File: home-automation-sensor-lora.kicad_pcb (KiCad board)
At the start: 4 copper layers, 96.5 x 96.5 mm, 126 parts, among them J1 Thermistor, J2 Conn_01x08, J3 Stemma-QT-Connector, J4 USB4105-GF-A_Lizard, J5 3V3-16V, J6 Conn_01x04, Q1 DMN2046U-7, Q2 DMN2046U-7, Q3 DMG3415U-7, U1 LD2985BM33R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

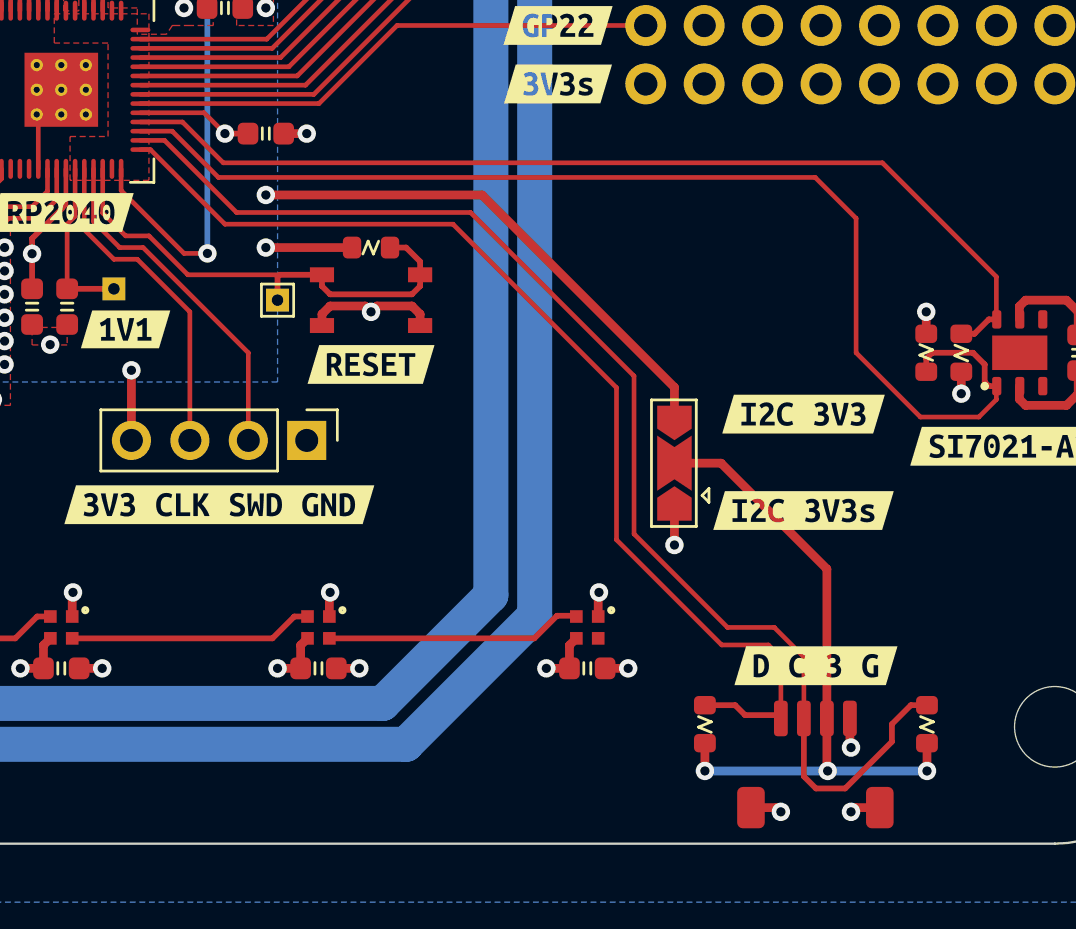
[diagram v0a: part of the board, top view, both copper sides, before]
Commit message: corrected mirrored stemma qt connector pinout
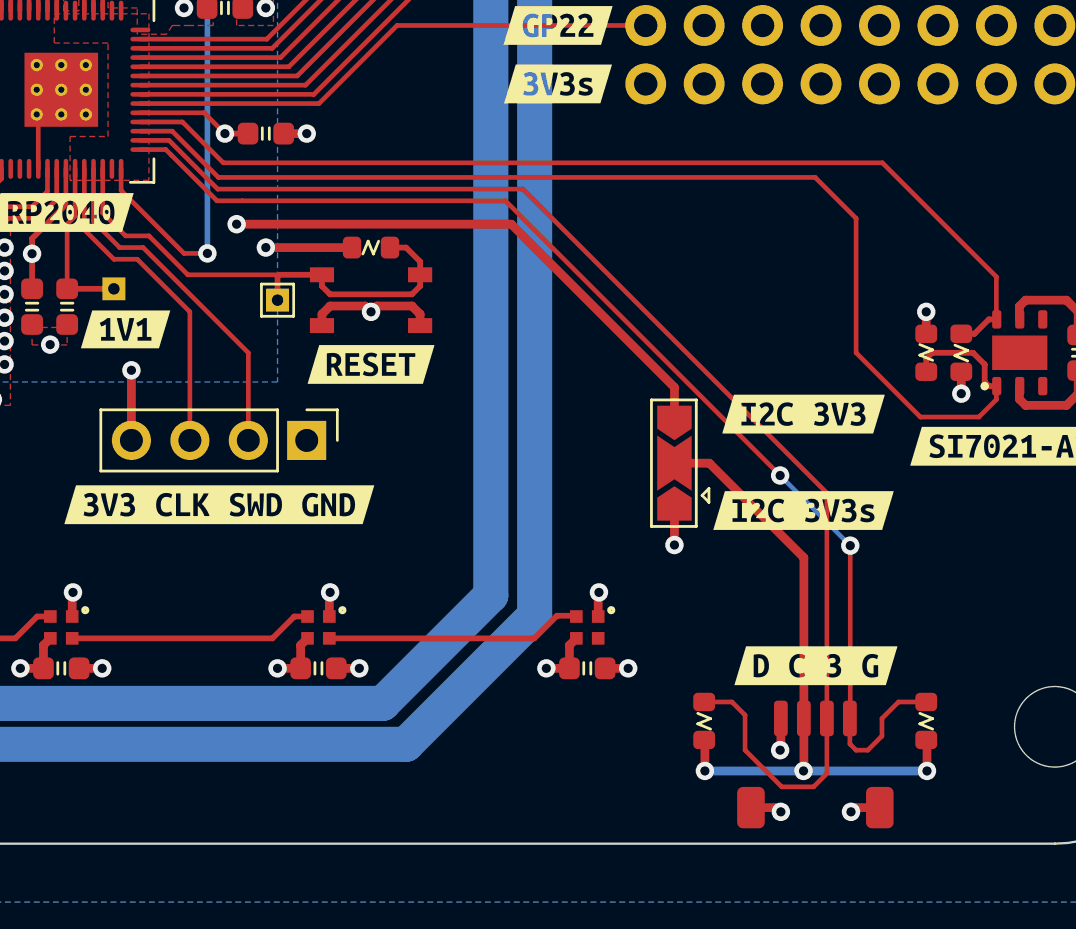
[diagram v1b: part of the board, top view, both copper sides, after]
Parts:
- moved R14 9.69 mm to (198.7, 122.5)
- moved R15 9.62 mm to (208.3, 122.5)
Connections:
- J3 pad 1: SDA1 -> GND
- J3 pad 2: SCL1 -> /QT Power
- J3 pad 3: /QT Power -> SCL1
- J3 pad 4: GND -> SDA1
- U5 pad 11: LORA_MISO -> unconnected-(U5-GPIO8-Pad11)
- U5 pad 4: unconnected-(U5-GPIO2-Pad4) -> LORA_RESET
- U5 pad 6: LORA_RESET -> LORA_MISO
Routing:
- net SDA1: track 46.8 -> 51.3 mm, vias 0 -> 2
- net SCL1: track 54.9 -> 56.4 mm
- net +3V3: track 53.3 -> 54.1 mm
- net /QT Power: track 29.4 -> 28.7 mm

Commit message: updated resistor values
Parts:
- R1, R10: value 1k -> 2k7
- R12: value 2.7k -> 2k7
- R14, R15: value 10k -> 2k7
- R5, R6, R7: value 5.1k -> 5k1
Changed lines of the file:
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@@
         (effects (font (size 1 1) (thickness 0.15)))
     )
-    (fp_text value "2.7k" (at 0 1.43) (layer "F.Fab")
+    (fp_text value "2k7" (at 0 1.43) (layer "F.Fab")
         (effects (font (size 1 1) (thickness 0.15)))
     )
@@
         (effects (font (size 1 1) (thickness 0.15)))
     )
-    (fp_text value "10k" (at 0 1.43 90) (layer "F.Fab")
+    (fp_text value "2k7" (at 0 1.43 90) (layer "F.Fab")
         (effects (font (size 1 1) (thickness 0.15)))
     )
@@
         (effects (font (size 1 1) (thickness 0.15)))
     )
-    (fp_text value "5.1k" (at 0 1.43 90) (layer "F.Fab")
+    (fp_text value "5k1" (at 0 1.43 90) (layer "F.Fab")
         (effects (font (size 1 1) (thickness 0.15)))
     )
@@
         (effects (font (size 1 1) (thickness 0.15)))
     )
-    (fp_text value "10k" (at 0 1.43 90) (layer "F.Fab")
+    (fp_text value "2k7" (at 0 1.43 90) (layer "F.Fab")
         (effects (font (size 1 1) (thickness 0.15)))
     )
@@
         (effects (font (size 1 1) (thickness 0.15)))
     )
-    (fp_text value "5.1k" (at 0 1.43 90) (layer "F.Fab")
+    (fp_text value "5k1" (at 0 1.43 90) (layer "F.Fab")
         (effects (font (size 1 1) (thickness 0.15)))
     )
@@
         (effects (font (size 1 1) (thickness 0.15)))
     )
-    (fp_text value "1k" (at 0 1.43) (layer "F.Fab")
+    (fp_text value "2k7" (at 0 1.43) (layer "F.Fab")
         (effects (font (size 1 1) (thickness 0.15)))
     )
@@
         (effects (font (size 1 1) (thickness 0.15)))
     )
-    (fp_text value "1k" (at 0 1.43) (layer "F.Fab")
+    (fp_text value "2k7" (at 0 1.43) (layer "F.Fab")
         (effects (font (size 1 1) (thickness 0.15)))
     )
@@
         (effects (font (size 1 1) (thickness 0.15)))
     )
-    (fp_text value "5.1k" (at 0 1.43 90) (layer "F.Fab")
+    (fp_text value "5k1" (at 0 1.43 90) (layer "F.Fab")
         (effects (font (size 1 1) (thickness 0.15)))
     )

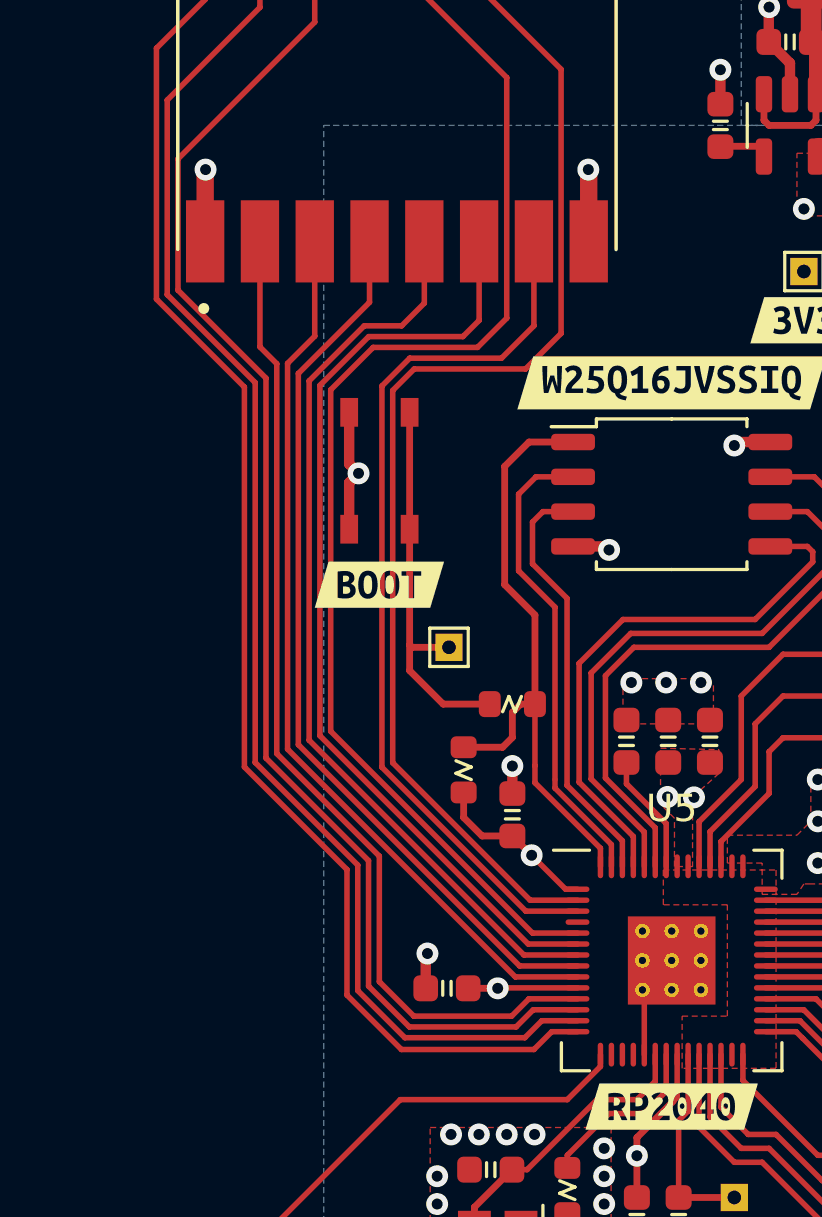
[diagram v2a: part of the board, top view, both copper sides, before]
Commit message: fixed routing to lora module
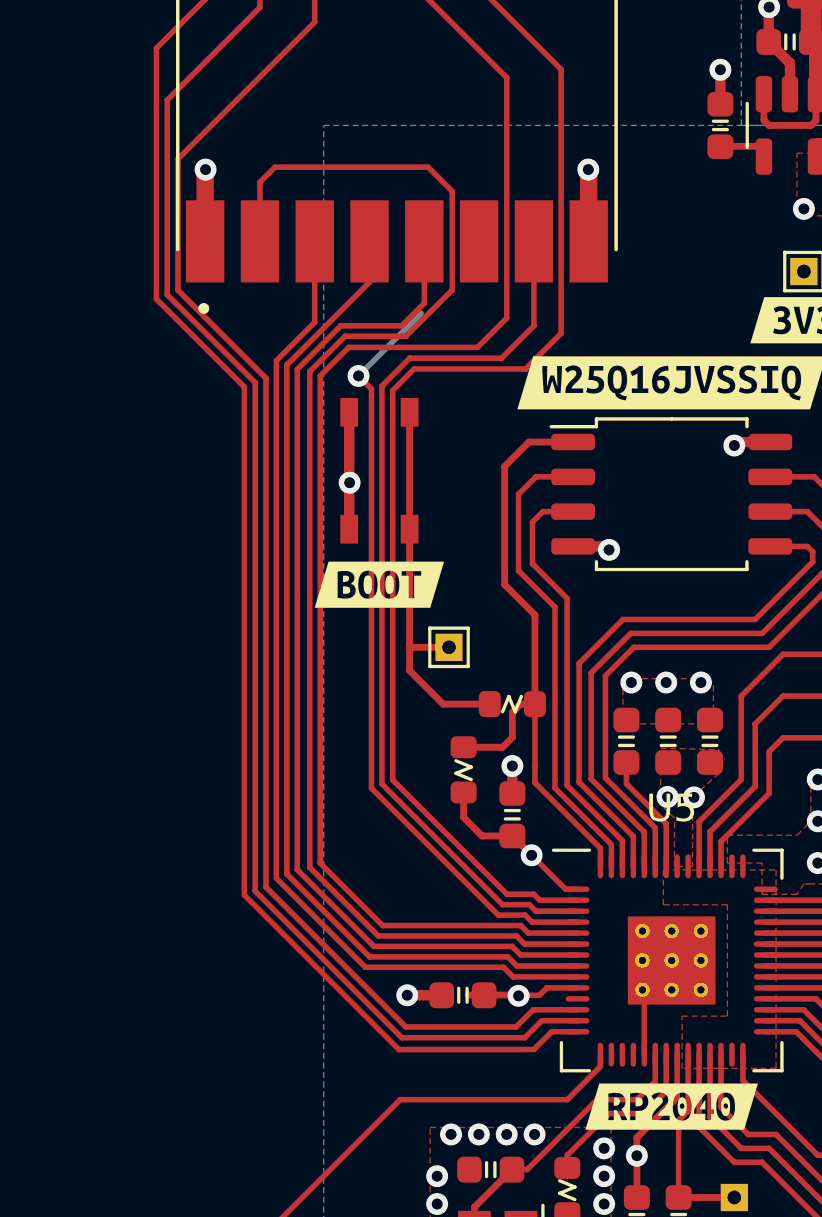
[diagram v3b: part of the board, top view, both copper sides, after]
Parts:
- moved C12 0.64 mm to (163.1, 96.3)
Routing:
- net LORA_MISO: track 36.8 -> 48.8 mm
- net LORA_RESET: track 35.0 -> 28.0 mm, vias 0 -> 1
- net LORA_NSS: track 33.8 -> 37.7 mm
- net LORA_DIO4: track 51.5 -> 55.4 mm
- net LORA_SCK: track 33.0 -> 36.3 mm
- net LORA_MOSI: track 33.0 -> 36.3 mm
- net GND: track 67.9 -> 67.4 mm

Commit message: updated BMS to auto-start version
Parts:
- U7: value AP9101CK6-ANTRG1 -> AP9101CAK6-ANTRG1
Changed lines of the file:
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@@
   (net 73 "unconnected-(U4-DNC-Pad4)")
   (net 74 "unconnected-(U4-PAD-Pad7)")
-  (net 75 "Net-(#FLG0103-pwr)")
+  (net 75 "Net-(U2-VIN)")
   (net 76 "unconnected-(U5-GPIO13-Pad16)")
   (net 77 "unconnected-(U5-GPIO14-Pad17)")
   (net 78 "unconnected-(U5-GPIO15-Pad18)")
   (net 79 "unconnected-(U5-GPIO16-Pad27)")
-  (net 80 "Net-(#FLG0101-pwr)")
+  (net 80 "Net-(U1-EN)")
   (net 81 "unconnected-(U5-GPIO8-Pad11)")
   (footprint "lizard_libs:R_0603_Lizard" (layer "F.Cu")
@@
       (stroke (width 0.1) (type solid)) (layer "F.Fab"))
     (pad "1" smd roundrect (at -1.1375 -0.95 270) (size 1.325 0.6) (layers "F.Cu" "F.Paste" "F.Mask") (roundrect_rratio 0.25)
-      (net 75 "Net-(#FLG0103-pwr)") (pinfunction "VIN") (pintype "power_in"))
+      (net 75 "Net-(U2-VIN)") (pinfunction "VIN") (pintype "power_in"))
     (pad "2" smd roundrect (at -1.1375 0 270) (size 1.325 0.6) (layers "F.Cu" "F.Paste" "F.Mask") (roundrect_rratio 0.25)
       (net 1 "GND") (pinfunction "GND") (pintype "power_in"))
@@
       (net 2 "VCC") (pintype "passive"))
     (pad "2" smd roundrect (at 1.4625 0 270) (size 1.125 1.75) (layers "F.Cu" "F.Paste" "F.Mask") (roundrect_rratio 0.222222)
-      (net 75 "Net-(#FLG0103-pwr)") (pintype "passive"))
+      (net 75 "Net-(U2-VIN)") (pintype "passive"))
     (model "${KICAD6_3DMODEL_DIR}/Resistor_SMD.3dshapes/R_1206_3216Metric.wrl"
       (offset (xyz 0 0 0))
@@
       (net 2 "VCC") (pintype "passive"))
     (pad "2" smd roundrect (at 1.4625 0 270) (size 1.125 1.75) (layers "F.Cu" "F.Paste" "F.Mask") (roundrect_rratio 0.222222)
-      (net 80 "Net-(#FLG0101-pwr)") (pintype "passive"))
+      (net 80 "Net-(U1-EN)") (pintype "passive"))
     (model "${KICAD6_3DMODEL_DIR}/Resistor_SMD.3dshapes/R_1206_3216Metric.wrl"
       (offset (xyz 0 0 0))
@@
         (effects (font (size 1 1) (thickness 0.15)))
     )
-    (fp_text value "AP9101CK6-ANTRG1" (at 0 2.4 90) (layer "F.Fab")
+    (fp_text value "AP9101CAK6-ANTRG1" (at 0 2.4 90) (layer "F.Fab")
         (effects (font (size 1 1) (thickness 0.15)))
     )
@@
       (stroke (width 0.1) (type solid)) (layer "F.Fab"))
     (pad "1" smd roundrect (at -1.1375 -0.95 270) (size 1.325 0.6) (layers "F.Cu" "F.Paste" "F.Mask") (roundrect_rratio 0.25)
-      (net 80 "Net-(#FLG0101-pwr)") (pinfunction "VIN") (pintype "power_in"))
+      (net 80 "Net-(U1-EN)") (pinfunction "VIN") (pintype "power_in"))
     (pad "2" smd roundrect (at -1.1375 0 270) (size 1.325 0.6) (layers "F.Cu" "F.Paste" "F.Mask") (roundrect_rratio 0.25)
       (net 1 "GND") (pinfunction "GND") (pintype "power_in"))
     (pad "3" smd roundrect (at -1.1375 0.95 270) (size 1.325 0.6) (layers "F.Cu" "F.Paste" "F.Mask") (roundrect_rratio 0.25)
-      (net 80 "Net-(#FLG0101-pwr)") (pinfunction "EN") (pintype "bidirectional"))
+      (net 80 "Net-(U1-EN)") (pinfunction "EN") (pintype "bidirectional"))
     (pad "4" smd roundrect (at 1.1375 0.95 270) (size 1.325 0.6) (layers "F.Cu" "F.Paste" "F.Mask") (roundrect_rratio 0.25)
       (net 11 "Net-(U1-BP)") (pinfunction "BP") (pintype "bidirectional"))
@@
       (stroke (width 0.1) (type solid)) (layer "F.Fab"))
     (pad "1" smd roundrect (at -0.775 0 180) (size 0.9 0.95) (layers "F.Cu" "F.Paste" "F.Mask") (roundrect_rratio 0.25)
-      (net 75 "Net-(#FLG0103-pwr)") (pintype "passive"))
+      (net 75 "Net-(U2-VIN)") (pintype "passive"))
     (pad "2" smd roundrect (at 0.775 0 180) (size 0.9 0.95) (layers "F.Cu" "F.Paste" "F.Mask") (roundrect_rratio 0.25)
       (net 1 "GND") (pintype "passive"))
@@
       (stroke (width 0.1) (type solid)) (layer "F.Fab"))
     (pad "1" smd roundrect (at -0.775 0 180) (size 0.9 0.95) (layers "F.Cu" "F.Paste" "F.Mask") (roundrect_rratio 0.25)
-      (net 80 "Net-(#FLG0101-pwr)") (pintype "passive"))
+      (net 80 "Net-(U1-EN)") (pintype "passive"))
     (pad "2" smd roundrect (at 0.775 0 180) (size 0.9 0.95) (layers "F.Cu" "F.Paste" "F.Mask") (roundrect_rratio 0.25)
       (net 1 "GND") (pintype "passive"))
